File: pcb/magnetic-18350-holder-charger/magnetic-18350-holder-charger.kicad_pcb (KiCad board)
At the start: 2 copper layers, 82 x 28.6 mm, 6 parts, among them U1 BatteryCharger4096, U2 MagneticInput, U3 18350-HOLDER

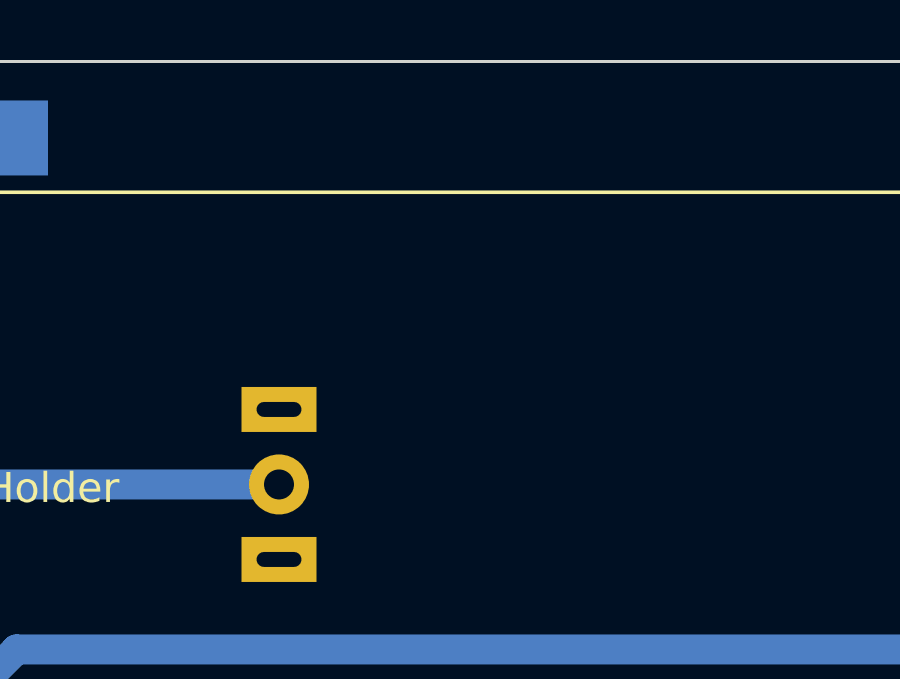
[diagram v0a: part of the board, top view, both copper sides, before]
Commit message: Added a pad to test vcc.
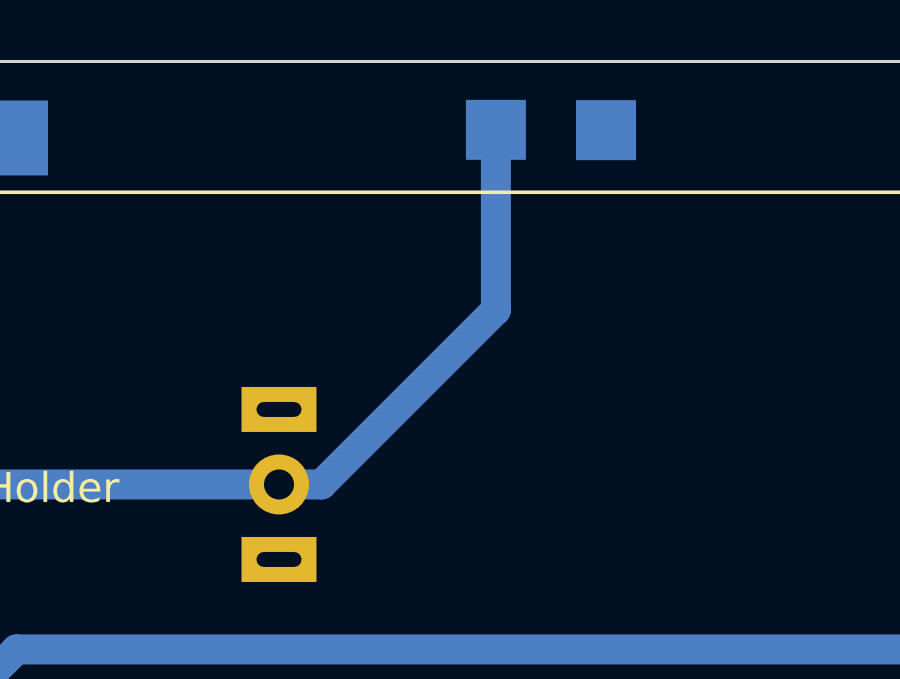
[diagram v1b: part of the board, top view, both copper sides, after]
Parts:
- added REF**: TestPoint_Pad_2.0x2.0mm, TestPoint:TestPoint_Pad_2.0x2.0mm, B.Cu at (149.9, 78.7)
- added REF**: TestPoint_Pad_2.0x2.0mm, TestPoint:TestPoint_Pad_2.0x2.0mm, B.Cu at (146.3, 78.7)
- added kibuzzard-63272079: G***, kibuzzard-63272079, B.Cu at (141.9, 78.7)
- added kibuzzard-63272085: G***, kibuzzard-63272085, B.Cu at (154.3, 78.7)
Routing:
- net Net-(U1-Pad3): track 28.4 -> 44.0 mm
